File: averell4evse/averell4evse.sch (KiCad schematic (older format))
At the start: 15 parts, among them J1 Conn_01x16, J2 Conn_01x13, J3 Conn_01x04, J4 Conn_01x03, J5 Conn_01x09, U1 KT2520K-T, U2 NFCv4, U3 TLC5957RTQ, U4 74AUC2G125, U5 touch_sensor

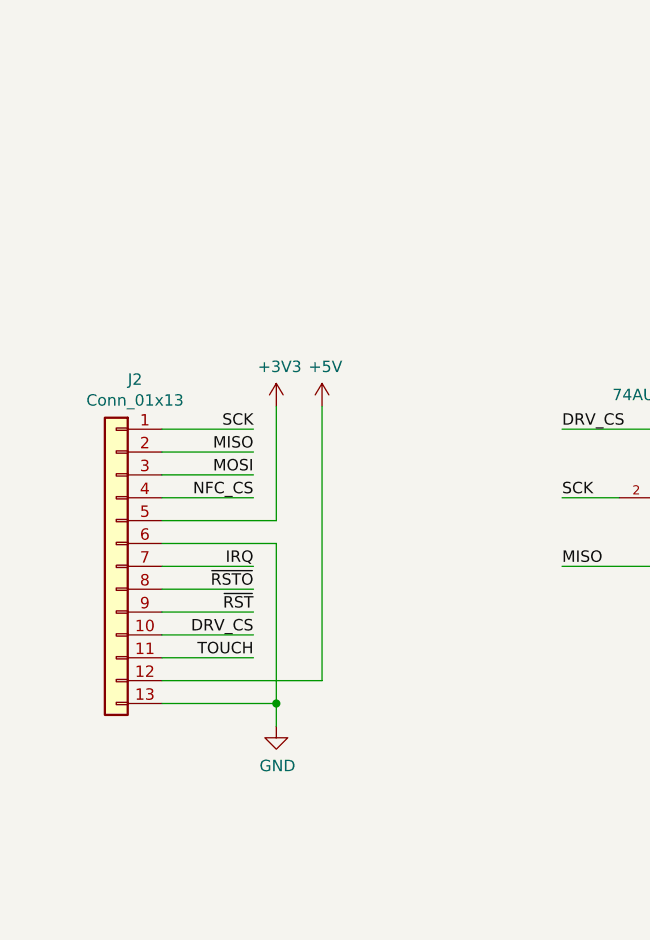
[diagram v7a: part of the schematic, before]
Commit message: averell/sch: Change Joe connector to RJ45
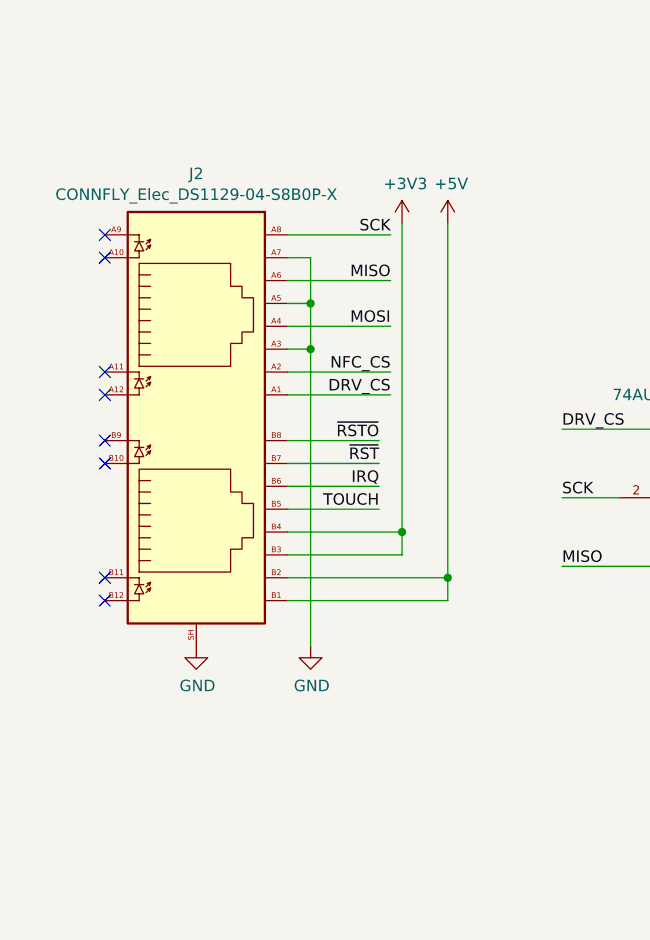
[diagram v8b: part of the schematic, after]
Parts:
- removed J2: Conn_01x13, Connector_PinHeader_2.54mm:PinHeader_1x13_P2.54mm_Horizontal, symbol Connector_Generic:Conn_01x13
- added J2: CONNFLY_Elec_DS1129-04-S8B0P-X, ma4evse:CONNFLY_Elec_DS1129-04-S8B0P-X, symbol ma4evse:CONNFLY_Elec_DS1129-04-S8B0P-X
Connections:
- net +3V3: now also J2.B3, J2.B4
- net +5V: now also J2.B1, J2.B2
- net DRV_CS: now also J2.A1
- net GND: now also J2.A3, J2.A5, J2.A7, J2.SH
- net IRQ: now also J2.B6
- net MISO: now also J2.A6
- net MOSI: now also J2.A4
- net NFC_CS: now also J2.A2
- net SCK: now also J2.A8
- net TOUCH: now also J2.B5
- net ~RST: now also J2.B7
- net ~RSTO: now also J2.B8
- no-connect marks 8 -> 16
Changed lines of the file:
@@
 Text Label 10900 5200 2    50   ~ 0
 ~RST
-Wire Wire Line
-	1100 3650 1500 3650
-Text Label 1500 3650 2    50   ~ 0
-SCK
-Wire Wire Line
-	1100 3850 1500 3850
-Text Label 1500 3850 2    50   ~ 0
-MOSI
-Wire Wire Line
-	1500 3750 1100 3750
-Text Label 1500 3750 2    50   ~ 0
-MISO
-Wire Wire Line
-	1100 4250 1500 4250
-Wire Wire Line
-	1100 4350 1500 4350
-Text Label 1500 4250 2    50   ~ 0
-IRQ
-Text Label 1500 4350 2    50   ~ 0
-~RSTO
-Wire Wire Line
-	1100 3950 1500 3950
-Text Label 1500 3950 2    50   ~ 0
-NFC_CS
-Wire Wire Line
-	1100 4450 1500 4450
-Text Label 1500 4450 2    50   ~ 0
-~RST
-Wire Wire Line
-	1100 4650 1500 4650
-Text Label 1500 4650 2    50   ~ 0
-TOUCH
-$Comp
-L power:+3V3 #PWR0121
-U 1 1 5DDA9C82
-P 1600 3550
-F 0 "#PWR0121" H 1600 3400 50  0001 C CNN
-F 1 "+3V3" H 1615 3723 50  0000 C CNN
-F 2 "" H 1600 3550 50  0001 C CNN
-F 3 "" H 1600 3550 50  0001 C CNN
-	1    1600 3550
-	1    0    0    -1
-$EndComp
-$Comp
-L power:+5V #PWR0122
-U 1 1 5DDB0D60
-P 1800 3550
-F 0 "#PWR0122" H 1800 3400 50  0001 C CNN
-F 1 "+5V" H 1815 3723 50  0000 C CNN
-F 2 "" H 1800 3550 50  0001 C CNN
-F 3 "" H 1800 3550 50  0001 C CNN
-	1    1800 3550
-	1    0    0    -1
-$EndComp
-$Comp
-L power:GND #PWR0123
-U 1 1 5DDB21AA
-P 1600 4950
-F 0 "#PWR0123" H 1600 4700 50  0001 C CNN
-F 1 "GND" H 1605 4777 50  0000 C CNN
-F 2 "" H 1600 4950 50  0001 C CNN
-F 3 "" H 1600 4950 50  0001 C CNN
-	1    1600 4950
-	1    0    0    -1
-$EndComp
-Wire Wire Line
-	1100 4150 1600 4150
-Wire Wire Line
-	1100 4850 1600 4850
-Connection ~ 1600 4850
-Wire Wire Line
-	1600 4850 1600 4950
-Wire Wire Line
-	1100 4050 1600 4050
-Wire Wire Line
-	1600 4050 1600 3550
-Wire Wire Line
-	1100 4750 1800 4750
 $Comp
 L Connector_Generic:Conn_01x16 J1
@@
 Wire Wire Line
 	4200 4200 4200 4400
-$Comp
-L Connector_Generic:Conn_01x13 J2
-U 1 1 5DFE7B6A
-P 900 4250
-F 0 "J2" H 818 5067 50  0000 C CNN
-F 1 "Conn_01x13" H 818 4976 50  0000 C CNN
-F 2 "Connector_PinHeader_2.54mm:PinHeader_1x13_P2.54mm_Horizontal" H 900 4250 50  0001 C CNN
-F 3 "~" H 900 4250 50  0001 C CNN
-	1    900  4250
-	-1   0    0    -1
-$EndComp
-Wire Wire Line
-	1600 4150 1600 4850
-Wire Wire Line
-	1800 3550 1800 4750
-Wire Wire Line
-	1100 4550 1500 4550
-Text Label 1500 4550 2    50   ~ 0
-DRV_CS
 Text Label 4500 3950 0    50   ~ 0
 DRV_SCK
+Text Label 2100 2800 2    50   ~ 0
+SCK
+Text Label 2100 3200 2    50   ~ 0
+MOSI
+Text Label 2100 3000 2    50   ~ 0
+MISO
+Text Label 2100 3400 2    50   ~ 0
+NFC_CS
+Text Label 2100 3500 2    50   ~ 0
+DRV_CS
+$Comp
+L power:GND #PWR013
+U 1 1 5E0E57F4
+P 1750 4600
+F 0 "#PWR013" H 1750 4350 50  0001 C CNN
+F 1 "GND" H 1755 4427 50  0000 C CNN
+F 2 "" H 1750 4600 50  0001 C CNN
+F 3 "" H 1750 4600 50  0001 C CNN
+	1    1750 4600
+	1    0    0    -1
+$EndComp
+Wire Wire Line
+	1750 2900 1750 3100
+Connection ~ 1750 3100
+Wire Wire Line
+	1750 3100 1750 3300
+Connection ~ 1750 3300
+Wire Wire Line
+	1750 3300 1750 4600
+NoConn ~ 850  2800
+NoConn ~ 850  2900
+NoConn ~ 850  3400
+NoConn ~ 850  3500
+Wire Wire Line
+	1650 3900 2050 3900
+Wire Wire Line
+	1650 3700 2050 3700
+Text Label 2050 3900 2    50   ~ 0
+IRQ
+Text Label 2050 3700 2    50   ~ 0
+~RSTO
+Wire Wire Line
+	1650 3800 2050 3800
+Text Label 2050 3800 2    50   ~ 0
+~RST
+Wire Wire Line
+	1650 4000 2050 4000
+Text Label 2050 4000 2    50   ~ 0
+TOUCH
+$Comp
+L power:+3V3 #PWR014
+U 1 1 5E19EC10
+P 2150 2750
+F 0 "#PWR014" H 2150 2600 50  0001 C CNN
+F 1 "+3V3" H 2165 2923 50  0000 C CNN
+F 2 "" H 2150 2750 50  0001 C CNN
+F 3 "" H 2150 2750 50  0001 C CNN
+	1    2150 2750
+	1    0    0    -1
+$EndComp
+$Comp
+L power:+5V #PWR015
+U 1 1 5E19EC16
+P 2350 2750
+F 0 "#PWR015" H 2350 2600 50  0001 C CNN
+F 1 "+5V" H 2365 2923 50  0000 C CNN
+F 2 "" H 2350 2750 50  0001 C CNN
+F 3 "" H 2350 2750 50  0001 C CNN
+	1    2350 2750
+	1    0    0    -1
+$EndComp
+Wire Wire Line
+	1650 4100 2150 4100
+Wire Wire Line
+	2150 4100 2150 2750
+Wire Wire Line
+	1650 4200 2150 4200
+Wire Wire Line
+	2150 4200 2150 4100
+Connection ~ 2150 4100
+Wire Wire Line
+	1650 4300 2350 4300
+Wire Wire Line
+	2350 4300 2350 2750
+Wire Wire Line
+	1650 4400 2350 4400
+Wire Wire Line
+	2350 4400 2350 4300
+Connection ~ 2350 4300
+NoConn ~ 850  3700
+NoConn ~ 850  3800
+NoConn ~ 850  4300
+NoConn ~ 850  4400
+$Comp
+L power:GND #PWR012
+U 1 1 5E293AEA
+P 1250 4600
+F 0 "#PWR012" H 1250 4350 50  0001 C CNN
+F 1 "GND" H 1255 4427 50  0000 C CNN
+F 2 "" H 1250 4600 50  0001 C CNN
+F 3 "" H 1250 4600 50  0001 C CNN
+	1    1250 4600
+	1    0    0    -1
+$EndComp
+$Comp
+L ma4evse:CONNFLY_Elec_DS1129-04-S8B0P-X J2
+U 1 1 5E2BD21A
+P 1250 3600
+F 0 "J2" H 1250 4667 50  0000 C CNN
+F 1 "CONNFLY_Elec_DS1129-04-S8B0P-X" H 1250 4576 50  0000 C CNN
+F 2 "ma4evse:CONNFLY_Elec_DS1129-04-S8B0P-X" V 2450 3750 50  0001 C CNN
+F 3 "https://datasheet.lcsc.com/szlcsc/1811141116_CONNFLY-Elec-DS1129-04-S8B0P-X_C86581.pdf" V 1250 4025 50  0001 C CNN
+	1    1250 3600
+	1    0    0    -1
+$EndComp
+Wire Wire Line
+	1650 2800 2100 2800
+Wire Wire Line
+	1650 3200 2100 3200
+Wire Wire Line
+	1650 3000 2100 3000
+Wire Wire Line
+	1650 3400 2100 3400
+Wire Wire Line
+	1650 3500 2100 3500
+Wire Wire Line
+	1650 2900 1750 2900
+Wire Wire Line
+	1650 3100 1750 3100
+Wire Wire Line
+	1650 3300 1750 3300
 Wire Bus Line
 	8250 1050 8250 3450
